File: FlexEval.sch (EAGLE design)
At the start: 173 parts, among them J1 USB4105-GF-A, J2 GRPB052VWQS-RC, SW1 1825910-7, U1 MK22FX512AVLQ12, U3 IS31FL3733B-TQLS4, U4 IS31FL3733B-TQLS4, U5 SOIC127P600X175-8N, U6 AP2115M-3.3TRG1, Y1 ABM3B-8.000MHZ-B2-T, Y2 ABS07-32.768KHZ-T

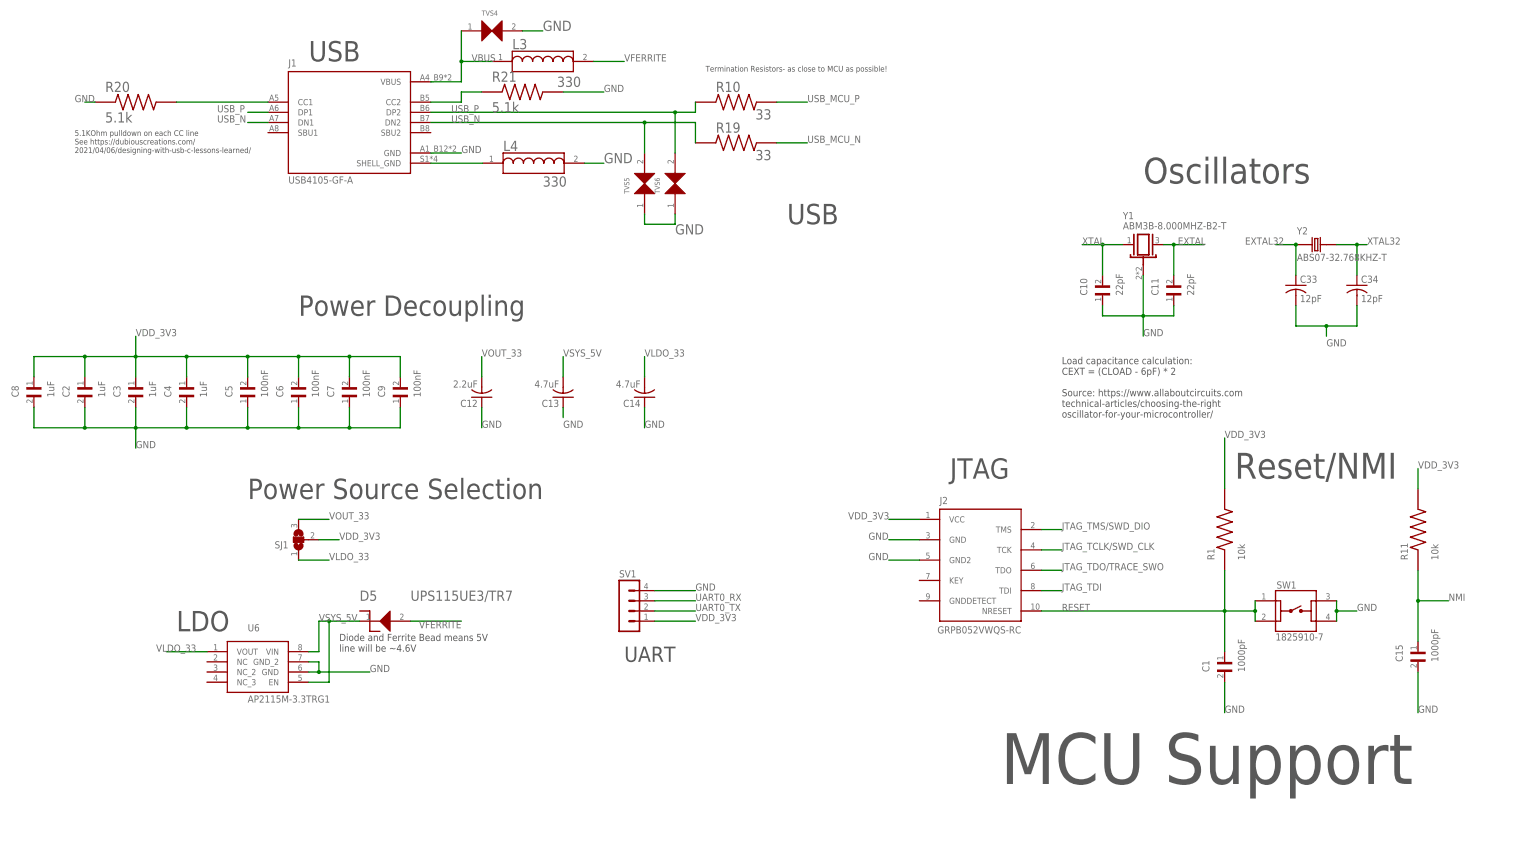
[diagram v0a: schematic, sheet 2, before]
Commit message: schematic: update resistors and capacitors to Eagle libraries
Updated all resistors and capacitors to use Eagle libraries instead
of custom SnapEDA variants for each component. This should improve
flexibility of the design, since SMD packages for passives are standard
sizes.

Signed-off-by: Daniel DeGrasse <daniel@degrasse.com>
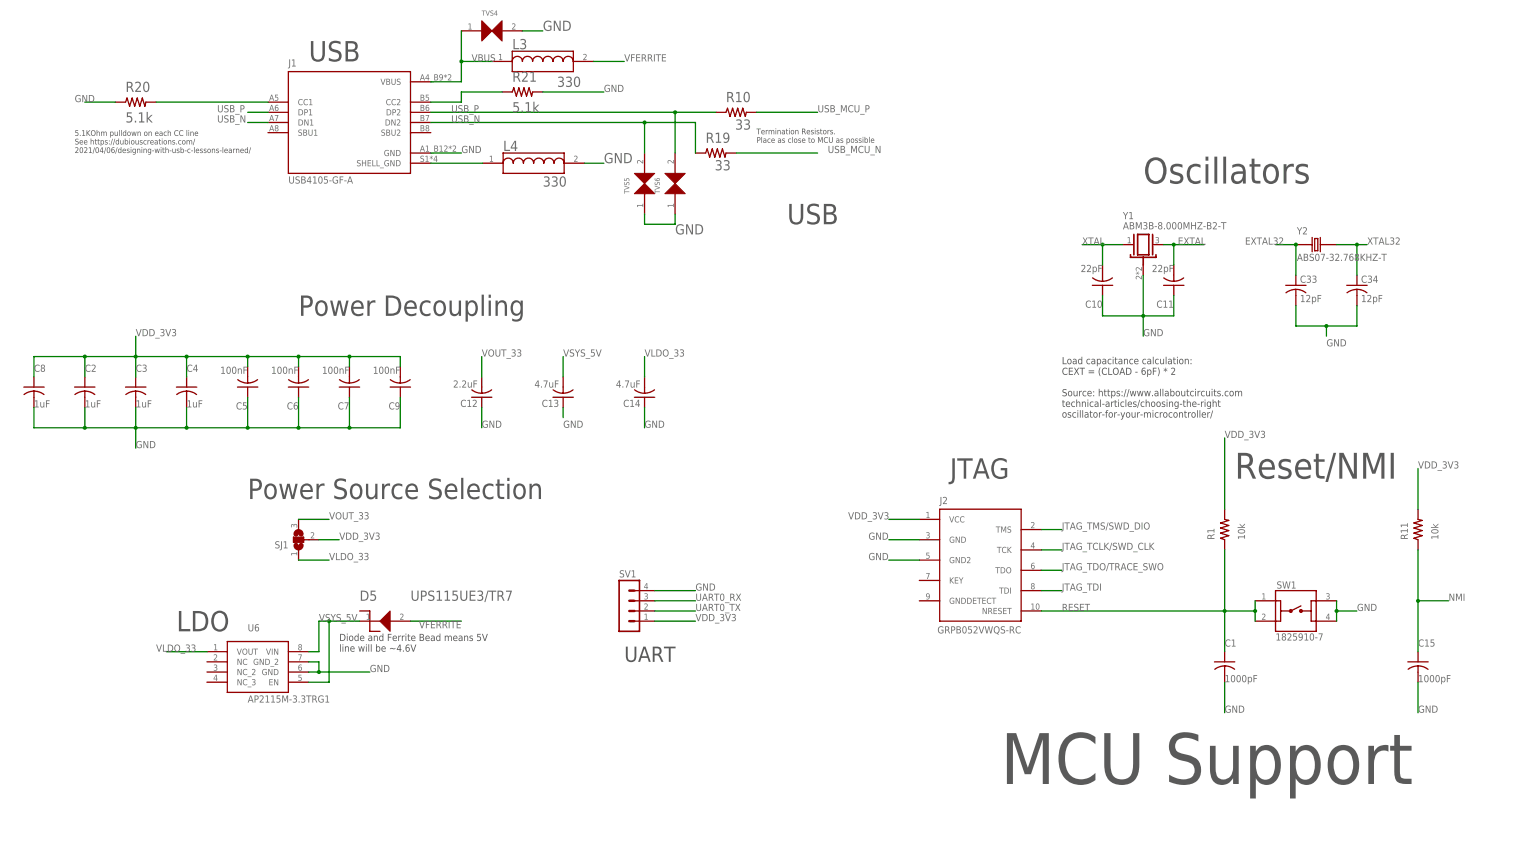
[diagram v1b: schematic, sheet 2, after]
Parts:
- C1, C15: device C1206C102K1RACAUTO:C1206C102K1RACAUTO -> resistor:C-USC1206
- C10, C11: device C1206C220JGGAC7800:C1206C220JGGAC7800 -> resistor:C-USC1206
- C2, C3, C4, C8: device GCM31MR71H105KA55L:GCM31MR71H105KA55L -> resistor:C-USC1206
- C5, C6, C7, C9: device C1206C104K5RAC7800:C1206C104K5RAC7800 -> resistor:C-USC1206
- R1, R11: device CRGCQ1206J10K:CRGCQ1206J10K -> resistor:R-US_R1206
- R10, R19: device CRG0805F33R:CRG0805F33R -> resistor:R-US_R0805
- R20, R21: device RNCP0805FTD20R0:RNCP0805FTD20R0 -> resistor:R-US_R0805
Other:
- note added: "Termination Resistors. Place as close to MCU as possible"
- note removed: "Termination Resistors- as close to MCU as possible!"
- moved on the sheet: C1, C10, C11, C15, C2, C3, C4, C5, C6, C7, C8, C9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

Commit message: board: replaced Electrolytic Capactitors
Replaced electrolytic capacitors with real models, instead of
Eagle's default library

Signed-off-by: Daniel DeGrasse <daniel@degrasse.com>
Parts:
- C23, C31: device resistor:CPOL-USE2.5-6 -> 860020672011:860020672011
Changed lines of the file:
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@@
 <part name="R4" library="resistor" library_urn="urn:adsk.eagle:library:348" deviceset="R-US_" device="R0805" package3d_urn="urn:adsk.eagle:package:23553/2" value="4.7K"/>
 <part name="R5" library="resistor" library_urn="urn:adsk.eagle:library:348" deviceset="R-US_" device="R0805" package3d_urn="urn:adsk.eagle:package:23553/2" value="4.7K"/>
-<part name="C23" library="resistor" library_urn="urn:adsk.eagle:library:348" deviceset="CPOL-US" device="E2.5-6" package3d_urn="urn:adsk.eagle:package:23349/1" value="22uF"/>
+<part name="C23" library="860020672011" deviceset="860020672011" device="" value="22uF"/>
 <part name="GND10" library="supply1" library_urn="urn:adsk.eagle:library:371" deviceset="GND" device=""/>
 <part name="R6" library="resistor" library_urn="urn:adsk.eagle:library:348" deviceset="R-US_" device="R0805" package3d_urn="urn:adsk.eagle:package:23553/2" value="100K"/>
@@
 <part name="GND2" library="supply1" library_urn="urn:adsk.eagle:library:371" deviceset="GND" device=""/>
 <part name="C30" library="resistor" library_urn="urn:adsk.eagle:library:348" deviceset="C-US" device="C0805" package3d_urn="urn:adsk.eagle:package:23617/2" value="0.47uF"/>
-<part name="C31" library="resistor" library_urn="urn:adsk.eagle:library:348" deviceset="CPOL-US" device="E2.5-6" package3d_urn="urn:adsk.eagle:package:23349/1" value="22uF"/>
+<part name="C31" library="860020672011" deviceset="860020672011" device="" value="22uF"/>
 <part name="R14" library="resistor" library_urn="urn:adsk.eagle:library:348" deviceset="R-US_" device="R0805" package3d_urn="urn:adsk.eagle:package:23553/2" value="100K"/>
 <part name="GND4" library="supply1" library_urn="urn:adsk.eagle:library:371" deviceset="GND" device=""/>
